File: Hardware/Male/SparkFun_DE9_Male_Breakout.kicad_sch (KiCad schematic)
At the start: 9 parts, among them J1 Conn_01x01, J2 Conn_01x09, J3 DE9 Male, J4 Conn_01x01

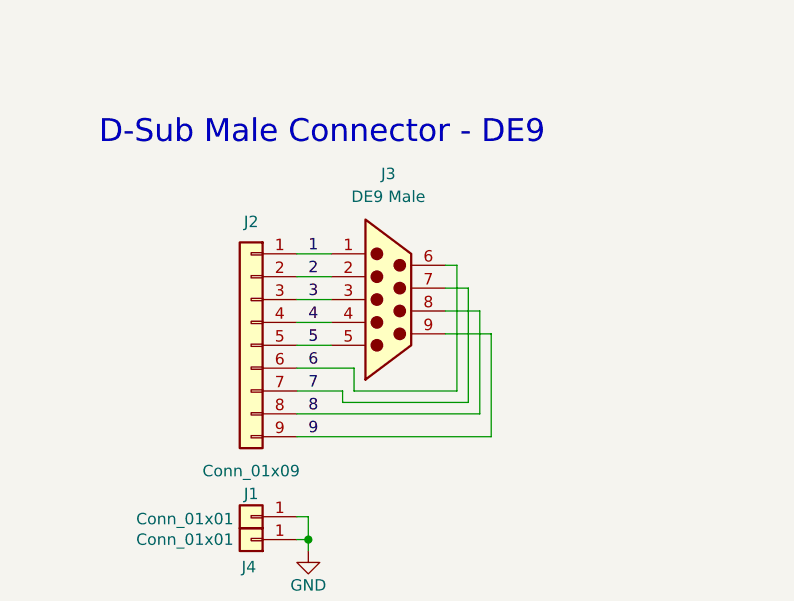
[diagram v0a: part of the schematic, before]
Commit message: Fixes silk and pinout on DE9 connector
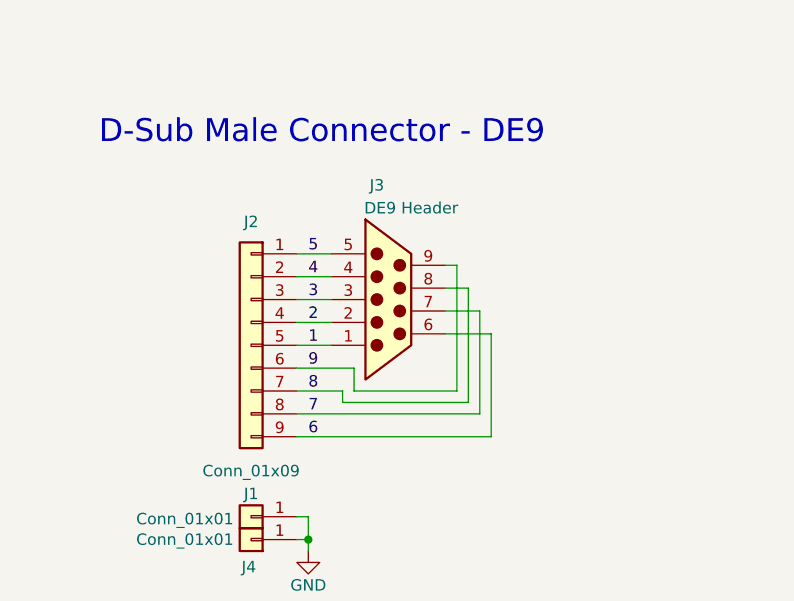
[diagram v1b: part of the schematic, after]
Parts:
- removed J3: DE9 Male, SparkFun-Connector:DE9_Male, symbol SparkFun-Connector:DE9_Male
- added J3: DE9 Header, SparkFun-Connector:DE9_Header_Horizontal_PTH, symbol SparkFun-Connector:DE9_Header_Horizontal_PTH
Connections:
- net 1: now also J2.5 (Pin_5), J3.1; no longer J2.1 (Pin_1)
- net 2: now also J2.4 (Pin_4), J3.2; no longer J2.2 (Pin_2)
- net 3: now also J3.3
- net 4: now also J2.2 (Pin_2), J3.4; no longer J2.4 (Pin_4)
- net 5: now also J2.1 (Pin_1), J3.5; no longer J2.5 (Pin_5)
- net 6: now also J2.9 (Pin_9), J3.6; no longer J2.6 (Pin_6)
- net 7: now also J2.8 (Pin_8), J3.7; no longer J2.7 (Pin_7)
- net 8: now also J2.7 (Pin_7), J3.8; no longer J2.8 (Pin_8)
- net 9: now also J2.6 (Pin_6), J3.9; no longer J2.9 (Pin_9)
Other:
- title: SparkFun DB9 Breakout -> SparkFun DE9 Breakout
